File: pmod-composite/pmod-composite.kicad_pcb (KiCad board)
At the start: 2 copper layers, 37.1 x 67.1 mm, 36 parts, among them J1 Conn_02x06_Top_Bottom, J2 PJRAN1X1U04X, J3 PJRAN1X1U04X, U1 NE5532

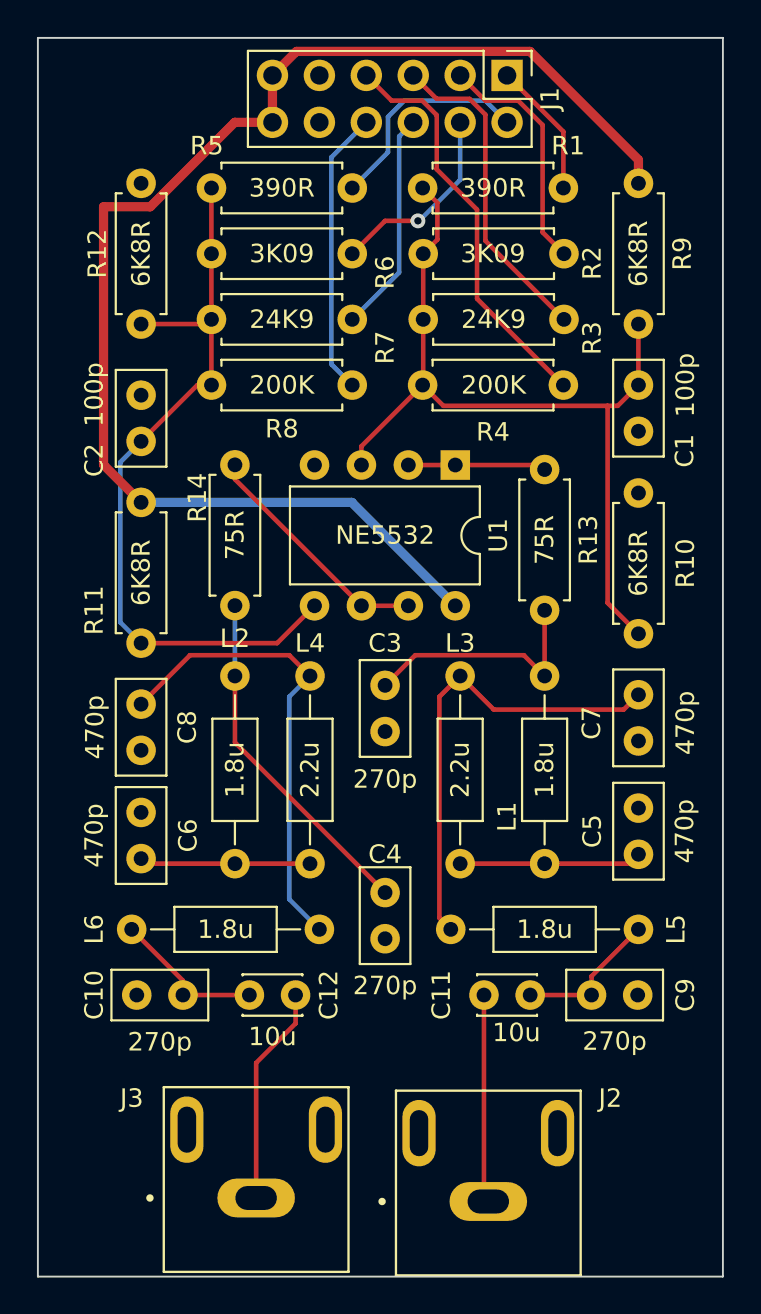
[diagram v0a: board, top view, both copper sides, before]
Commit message: relocate README.
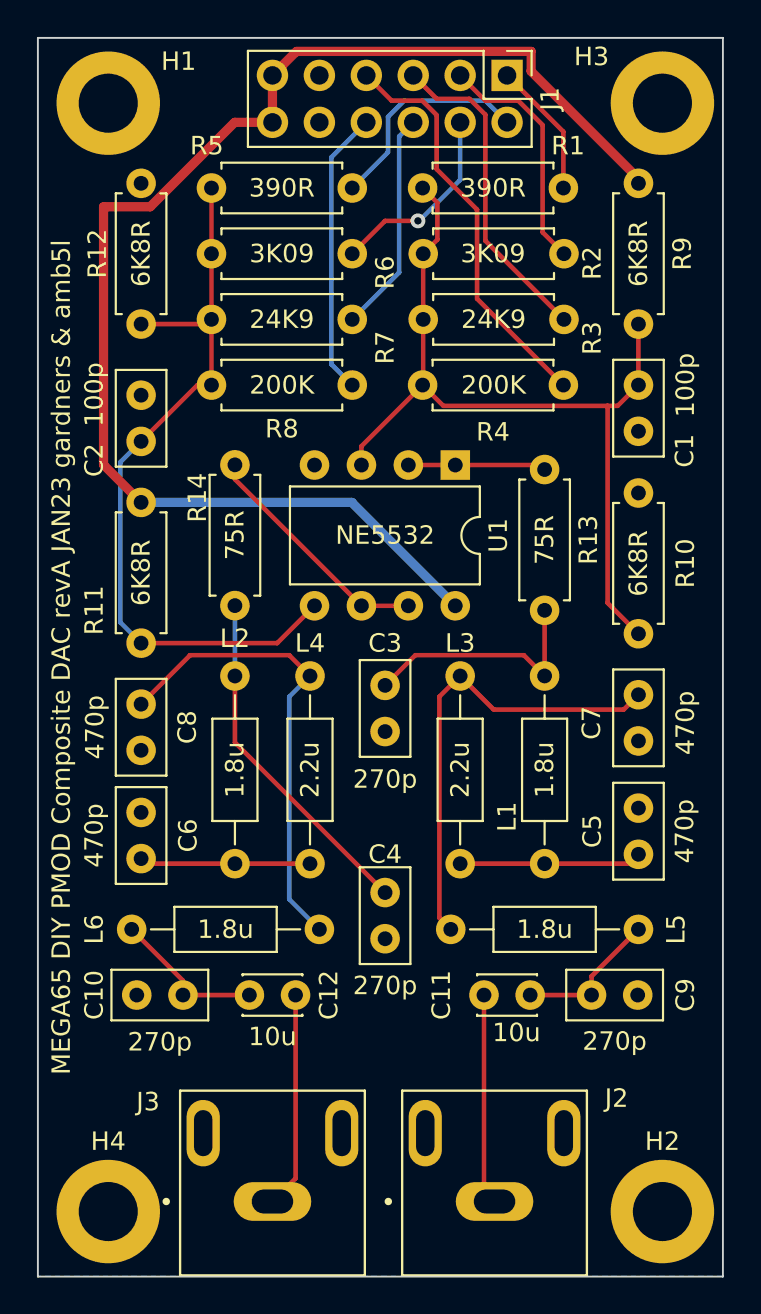
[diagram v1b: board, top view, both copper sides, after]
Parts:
- added H1: MountingHole_Pad, MountingHole:MountingHole_3.2mm_M3_DIN965_Pad, F.Cu at (29.2, 33.0)
- added H2: MountingHole_Pad, MountingHole:MountingHole_3.2mm_M3_DIN965_Pad, F.Cu at (59.2, 93.0)
- added H3: MountingHole_Pad, MountingHole:MountingHole_3.2mm_M3_DIN965_Pad, F.Cu at (58.9, 33.0)
- added H4: MountingHole_Pad, MountingHole:MountingHole_3.2mm_M3_DIN965_Pad, F.Cu at (29.2, 93.0)
- moved J3 0.90 mm to (38.1, 92.5)
- moved J2 0.34 mm to (50.1, 92.5)
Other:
- board text added: "MEGA65 DIY PMOD Composite DAC revA JAN23 gardners & amb5l"
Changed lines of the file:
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@@
   (net 23 "Net-(R13-Pad1)")
   (net 24 "Net-(R14-Pad1)")
+  (net 25 "unconnected-(H1-Pad1)")
+  (net 26 "unconnected-(H2-Pad1)")
+  (net 27 "unconnected-(H3-Pad1)")
+  (net 28 "unconnected-(H4-Pad1)")
+  (footprint "MountingHole:MountingHole_3.2mm_M3_DIN965_Pad" (layer "F.Cu")
+    (at 59.21 93)
+    (descr "Mounting Hole 3.2mm, M3, DIN965")
+    (tags "mounting hole 3.2mm m3 din965")
+    (property "Sheetfile" "pmod-composite.kicad_sch")
+    (property "Sheetname" "")
+    (attr exclude_from_pos_files)
+    (fp_text reference "H2" (at 0 -3.8) (layer "F.SilkS")
+      (effects (font (size 1 1) (thickness 0.15)))
+    )
+    (fp_text value "MountingHole_Pad" (at 0 3.8) (layer "F.Fab")
+      (effects (font (size 1 1) (thickness 0.15)))
+    )
+    (fp_text user "${REFERENCE}" (at 0 0) (layer "F.Fab")
+      (effects (font (size 1 1) (thickness 0.15)))
+    )
+    (fp_circle (center 0 0) (end 2.8 0) (layer "Cmts.User") (width 0.15) (fill none))
+    (fp_circle (center 0 0) (end 3.05 0) (layer "F.CrtYd") (width 0.05) (fill none))
+    (pad "1" thru_hole circle (at 0 0) (size 5.6 5.6) (drill 3.2) (layers *.Cu *.Mask)
+      (net 26 "unconnected-(H2-Pad1)") (pinfunction "1") (pintype "input"))
+  )
   (footprint "Capacitor_THT:C_Disc_D5.0mm_W2.5mm_P2.50mm" (layer "F.Cu")
     (at 44.196 75.732 -90)
@@
   )
   (footprint "00Project:SWITCHCRAFT_PJRAN1X1U04X" (layer "F.Cu")
-    (at 49.784 92.456)
+    (at 50.1215 92.456)
     (property "DigikeyPart" "PJRAN1X1U04X-ND")
     (property "MANUFACTURER" "Switchcraft")
@@
   )
   (footprint "00Project:SWITCHCRAFT_PJRAN1X1U04X" (layer "F.Cu")
-    (at 37.2165 92.266)
+    (at 38.1 92.456)
     (property "DigikeyPart" "PJRAN1X1U04X-ND")
     (property "MANUFACTURER" "Switchcraft")
@@
       (rotate (xyz 0 0 0))
     )
+  )
+  (footprint "MountingHole:MountingHole_3.2mm_M3_DIN965_Pad" (layer "F.Cu")
+    (at 58.928 33.02)
+    (descr "Mounting Hole 3.2mm, M3, DIN965")
+    (tags "mounting hole 3.2mm m3 din965")
+    (property "Sheetfile" "pmod-composite.kicad_sch")
+    (property "Sheetname" "")
+    (attr exclude_from_pos_files)
+    (fp_text reference "H3" (at -3.556 -2.54) (layer "F.SilkS")
+      (effects (font (size 1 1) (thickness 0.15)))
+    )
+    (fp_text value "MountingHole_Pad" (at 0 3.8) (layer "F.Fab")
+      (effects (font (size 1 1) (thickness 0.15)))
+    )
+    (fp_text user "${REFERENCE}" (at 0 0) (layer "F.Fab")
+      (effects (font (size 1 1) (thickness 0.15)))
+    )
+    (fp_circle (center 0 0) (end 2.8 0) (layer "Cmts.User") (width 0.15) (fill none))
+    (fp_circle (center 0 0) (end 3.05 0) (layer "F.CrtYd") (width 0.05) (fill none))
+    (pad "1" thru_hole circle (at 0.282 -0.02) (size 5.6 5.6) (drill 3.2) (layers *.Cu *.Mask)
+      (net 27 "unconnected-(H3-Pad1)") (pinfunction "1") (pintype "input"))
   )
   (footprint "Inductor_THT:L_Axial_L5.3mm_D2.2mm_P10.16mm_Horizontal_Vishay_IM-1" (layer "F.Cu")
@@
     )
   )
+  (footprint "MountingHole:MountingHole_3.2mm_M3_DIN965_Pad" (layer "F.Cu")
+    (at 29.21 33.02)
+    (descr "Mounting Hole 3.2mm, M3, DIN965")
+    (tags "mounting hole 3.2mm m3 din965")
+    (property "Sheetfile" "pmod-composite.kicad_sch")
+    (property "Sheetname" "")
+    (attr exclude_from_pos_files)
+    (fp_text reference "H1" (at 3.81 -2.286) (layer "F.SilkS")
+      (effects (font (size 1 1) (thickness 0.15)))
+    )
+    (fp_text value "MountingHole_Pad" (at 0 3.8) (layer "F.Fab")
+      (effects (font (size 1 1) (thickness 0.15)))
+    )
+    (fp_text user "${REFERENCE}" (at 0 0) (layer "F.Fab")
+      (effects (font (size 1 1) (thickness 0.15)))
+    )
+    (fp_circle (center 0 0) (end 2.8 0) (layer "Cmts.User") (width 0.15) (fill none))
+    (fp_circle (center 0 0) (end 3.05 0) (layer "F.CrtYd") (width 0.05) (fill none))
+    (pad "1" thru_hole circle (at 0 -0.02) (size 5.6 5.6) (drill 3.2) (layers *.Cu *.Mask)
+      (net 25 "unconnected-(H1-Pad1)") (pinfunction "1") (pintype "input"))
+  )
   (footprint "Capacitor_THT:C_Disc_D3.0mm_W2.0mm_P2.50mm" (layer "F.Cu")
     (at 52.05 81.28 180)
@@
     )
   )
+  (footprint "MountingHole:MountingHole_3.2mm_M3_DIN965_Pad" (layer "F.Cu")
+    (at 29.21 93)
+    (descr "Mounting Hole 3.2mm, M3, DIN965")
+    (tags "mounting hole 3.2mm m3 din965")
+    (property "Sheetfile" "pmod-composite.kicad_sch")
+    (property "Sheetname" "")
+    (attr exclude_from_pos_files)
+    (fp_text reference "H4" (at 0 -3.8) (layer "F.SilkS")
+      (effects (font (size 1 1) (thickness 0.15)))
+    )
+    (fp_text value "MountingHole_Pad" (at 0 3.8) (layer "F.Fab")
+      (effects (font (size 1 1) (thickness 0.15)))
+    )
+    (fp_text user "${REFERENCE}" (at 0 0) (layer "F.Fab")
+      (effects (font (size 1 1) (thickness 0.15)))
+    )
+    (fp_circle (center 0 0) (end 2.8 0) (layer "Cmts.User") (width 0.15) (fill none))
+    (fp_circle (center 0 0) (end 3.05 0) (layer "F.CrtYd") (width 0.05) (fill none))
+    (pad "1" thru_hole circle (at 0 0) (size 5.6 5.6) (drill 3.2) (layers *.Cu *.Mask)
+      (net 28 "unconnected-(H4-Pad1)") (pinfunction "1") (pintype "input"))
+  )
   (footprint "Capacitor_THT:C_Disc_D5.0mm_W2.5mm_P2.50mm" (layer "F.Cu")
     (at 44.196 64.516 -90)
@@
   )
   (gr_rect (start 25.4 29.464) (end 62.484 96.52) (layer "Edge.Cuts") (width 0.1) (fill none))
+  (gr_text "MEGA65 DIY PMOD Composite DAC revA JAN23 gardners & amb5l" (at 26.67 62.992 90) (layer "F.SilkS")
+    (effects (font (size 1 1) (thickness 0.15)))
+  )
   (segment (start 45.828511 62.883489) (end 44.196 64.516) (width 0.25) (layer "F.Cu") (net 1))
   (segment (start 52.832 60.452) (end 52.832 64.008) (width 0.25) (layer "F.Cu") (net 1))
@@
   (segment (start 49.55 92.222) (end 49.784 92.456) (width 0.25) (layer "F.Cu") (net 6))
   (segment (start 49.55 81.28) (end 49.55 92.222) (width 0.25) (layer "F.Cu") (net 6))
-  (segment (start 37.2165 84.9575) (end 37.2165 92.266) (width 0.25) (layer "F.Cu") (net 7))
-  (segment (start 39.35 82.824) (end 37.2165 84.9575) (width 0.25) (layer "F.Cu") (net 7))
-  (segment (start 39.35 81.28) (end 39.35 82.824) (width 0.25) (layer "F.Cu") (net 7))
+  (segment (start 39.35 91.206) (end 38.1 92.456) (width 0.25) (layer "F.Cu") (net 7))
+  (segment (start 39.35 81.28) (end 39.35 91.206) (width 0.25) (layer "F.Cu") (net 7))
   (segment (start 50.8 31.496) (end 53.848 34.544) (width 0.25) (layer "F.Cu") (net 8))
   (segment (start 53.848 34.544) (end 53.848 37.592) (width 0.25) (layer "F.Cu") (net 8))
@@
   (segment (start 31.485076 38.608) (end 36.057076 34.036) (width 0.5) (layer "F.Cu") (net 12))
   (segment (start 36.057076 34.036) (end 38.1 34.036) (width 0.5) (layer "F.Cu") (net 12))
+  (segment (start 39.399511 30.196489) (end 52.099511 30.196489) (width 0.5) (layer "F.Cu") (net 12))
+  (segment (start 57.912 37.084) (end 57.912 37.338) (width 0.5) (layer "F.Cu") (net 12))
   (segment (start 38.1 31.496) (end 39.399511 30.196489) (width 0.5) (layer "F.Cu") (net 12))
-  (segment (start 39.399511 30.196489) (end 52.040489 30.196489) (width 0.5) (layer "F.Cu") (net 12))
+  (segment (start 52.099511 31.271511) (end 57.912 37.084) (width 0.5) (layer "F.Cu") (net 12))
+  (segment (start 52.099511 30.196489) (end 52.099511 31.271511) (width 0.5) (layer "F.Cu") (net 12))
   (segment (start 38.1 34.036) (end 38.1 31.496) (width 0.5) (layer "F.Cu") (net 12))
-  (segment (start 57.912 36.068) (end 57.912 37.338) (width 0.5) (layer "F.Cu") (net 12))
   (segment (start 28.956 38.608) (end 31.485076 38.608) (width 0.5) (layer "F.Cu") (net 12))
   (segment (start 28.956 52.578) (end 28.956 38.608) (width 0.5) (layer "F.Cu") (net 12))
-  (segment (start 52.040489 30.196489) (end 57.912 36.068) (width 0.5) (layer "F.Cu") (net 12))
   (segment (start 30.988 54.61) (end 28.956 52.578) (width 0.5) (layer "F.Cu") (net 12))
   (segment (start 42.398 54.61) (end 47.996 60.208) (width 0.5) (layer "B.Cu") (net 12))
